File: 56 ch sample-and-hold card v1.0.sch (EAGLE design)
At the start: 124 parts, among them IC1 4051D, IC10 TL074JT, IC11 4051D, IC12 TL074JT, IC13 TL074JT, IC14 4051D, IC15 TL074JT, IC16 TL074JT, IC17 4051D, IC18 TL074JT, IC19 TL074JT, IC2 DAC8586D, IC20 4051D, IC21 TL074JT, IC22 TL074JT, IC26 4051D, IC27 TL074JT, IC28 TL074JT, IC3 TL074JT, IC5 78L05F, IC6 TL074JT, IC7 4051D, IC9 TL074JT, X2 FEMALE, X3 FEMALE, X4 FEMALE, X5 DNM, X6 DNM

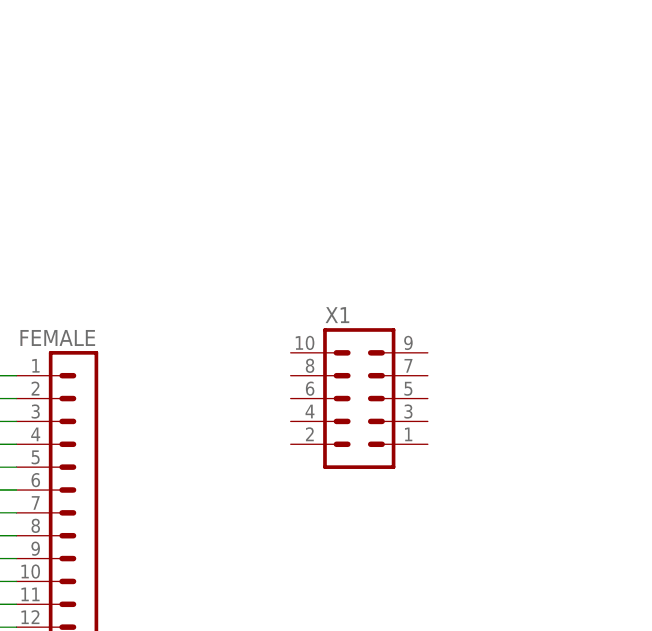
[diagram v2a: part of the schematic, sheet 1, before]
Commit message: All routed, nothing tested
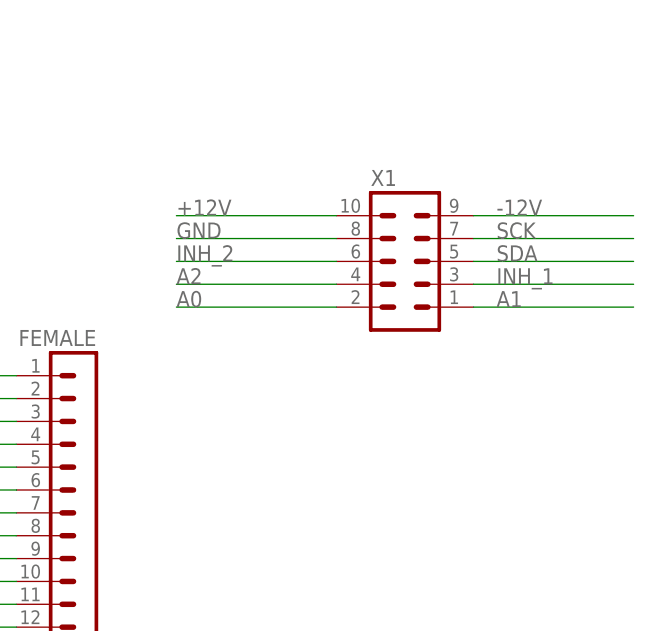
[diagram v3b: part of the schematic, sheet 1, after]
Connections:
- new net GND: X1.8
- net +12V: now also X1.10
- net -12V: now also X1.9
- net A0: now also X1.2
- net A1: now also X1.1
- net A2: now also X1.4
- net INH_1: now also X1.3
- net INH_2: now also X1.6
- net SCK: now also X1.7
- net SDA: now also X1.5
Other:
- moved on the sheet: X1
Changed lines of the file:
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@@
 <attribute name="VALUE" x="-2.54" y="71.12" size="1.778" layer="96"/>
 </instance>
-<instance part="X1" gate="G$1" x="129.54" y="-20.32" smashed="yes">
-<attribute name="VALUE" x="125.73" y="-30.48" size="1.778" layer="96"/>
-<attribute name="NAME" x="125.73" y="-11.938" size="1.778" layer="95"/>
+<instance part="X1" gate="G$1" x="134.62" y="-5.08" smashed="yes">
+<attribute name="VALUE" x="130.81" y="-15.24" size="1.778" layer="96"/>
+<attribute name="NAME" x="130.81" y="3.302" size="1.778" layer="95"/>
 </instance>
 <instance part="X2" gate="G$1" x="38.1" y="-35.56" smashed="yes" rot="R180">
@@
 <label x="55.88" y="22.86" size="1.778" layer="95"/>
 </segment>
+<segment>
+<pinref part="X1" gate="G$1" pin="9"/>
+<wire x1="142.24" y1="0" x2="160.02" y2="0" width="0.1524" layer="91"/>
+<label x="144.78" y="0" size="1.778" layer="95"/>
+</segment>
 </net>
 <net name="OUT_7" class="0">
@@
 <label x="55.88" y="25.4" size="1.778" layer="95"/>
 </segment>
+<segment>
+<pinref part="X1" gate="G$1" pin="10"/>
+<wire x1="127" y1="0" x2="109.22" y2="0" width="0.1524" layer="91"/>
+<label x="109.22" y="0" size="1.778" layer="95"/>
+</segment>
 </net>
 <net name="SCK" class="0">
@@
 <label x="55.88" y="17.78" size="1.778" layer="95"/>
 </segment>
+<segment>
+<pinref part="X1" gate="G$1" pin="7"/>
+<wire x1="142.24" y1="-2.54" x2="160.02" y2="-2.54" width="0.1524" layer="91"/>
+<label x="144.78" y="-2.54" size="1.778" layer="95"/>
+</segment>
 </net>
 <net name="SDA" class="0">
@@
 <label x="55.88" y="15.24" size="1.778" layer="95"/>
 </segment>
+<segment>
+<pinref part="X1" gate="G$1" pin="5"/>
+<wire x1="142.24" y1="-5.08" x2="160.02" y2="-5.08" width="0.1524" layer="91"/>
+<label x="144.78" y="-5.08" size="1.778" layer="95"/>
+</segment>
 </net>
 <net name="N$8" class="0">
@@
 <label x="55.88" y="7.62" size="1.778" layer="95"/>
 </segment>
+<segment>
+<pinref part="X1" gate="G$1" pin="2"/>
+<wire x1="127" y1="-10.16" x2="109.22" y2="-10.16" width="0.1524" layer="91"/>
+<label x="109.22" y="-10.16" size="1.778" layer="95"/>
+</segment>
 </net>
 <net name="A1" class="0">
@@
 <label x="55.88" y="5.08" size="1.778" layer="95"/>
 </segment>
+<segment>
+<pinref part="X1" gate="G$1" pin="1"/>
+<wire x1="142.24" y1="-10.16" x2="160.02" y2="-10.16" width="0.1524" layer="91"/>
+<label x="144.78" y="-10.16" size="1.778" layer="95"/>
+</segment>
 </net>
 <net name="A2" class="0">
@@
 <label x="55.88" y="2.54" size="1.778" layer="95"/>
 </segment>
+<segment>
+<pinref part="X1" gate="G$1" pin="4"/>
+<wire x1="127" y1="-7.62" x2="109.22" y2="-7.62" width="0.1524" layer="91"/>
+<label x="109.22" y="-7.62" size="1.778" layer="95"/>
+</segment>
 </net>
 <net name="INH_1" class="0">
@@
 <label x="55.88" y="0" size="1.778" layer="95"/>
 </segment>
+<segment>
+<pinref part="X1" gate="G$1" pin="3"/>
+<wire x1="142.24" y1="-7.62" x2="160.02" y2="-7.62" width="0.1524" layer="91"/>
+<label x="144.78" y="-7.62" size="1.778" layer="95"/>
+</segment>
 </net>
 <net name="INH_2" class="0">
@@
 <wire x1="55.88" y1="-2.54" x2="86.36" y2="-2.54" width="0.1524" layer="91"/>
 <label x="55.88" y="-2.54" size="1.778" layer="95"/>
+</segment>
+<segment>
+<pinref part="X1" gate="G$1" pin="6"/>
+<wire x1="127" y1="-5.08" x2="109.22" y2="-5.08" width="0.1524" layer="91"/>
+<label x="109.22" y="-5.08" size="1.778" layer="95"/>
 </segment>
 </net>
@@
 </segment>
 </net>
+<net name="GND" class="0">
+<segment>
+<pinref part="X1" gate="G$1" pin="8"/>
+<wire x1="127" y1="-2.54" x2="109.22" y2="-2.54" width="0.1524" layer="91"/>
+<label x="109.22" y="-2.54" size="1.778" layer="95"/>
+</segment>
+</net>

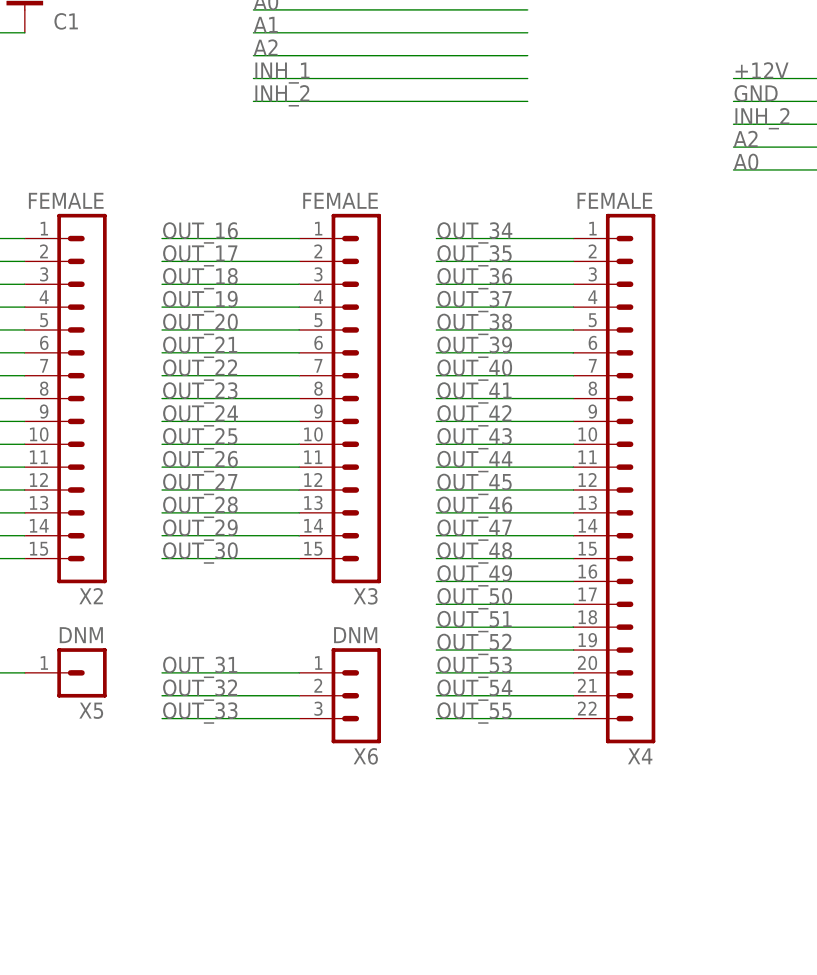
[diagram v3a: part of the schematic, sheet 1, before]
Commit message: Split 22p into 15p and 7p
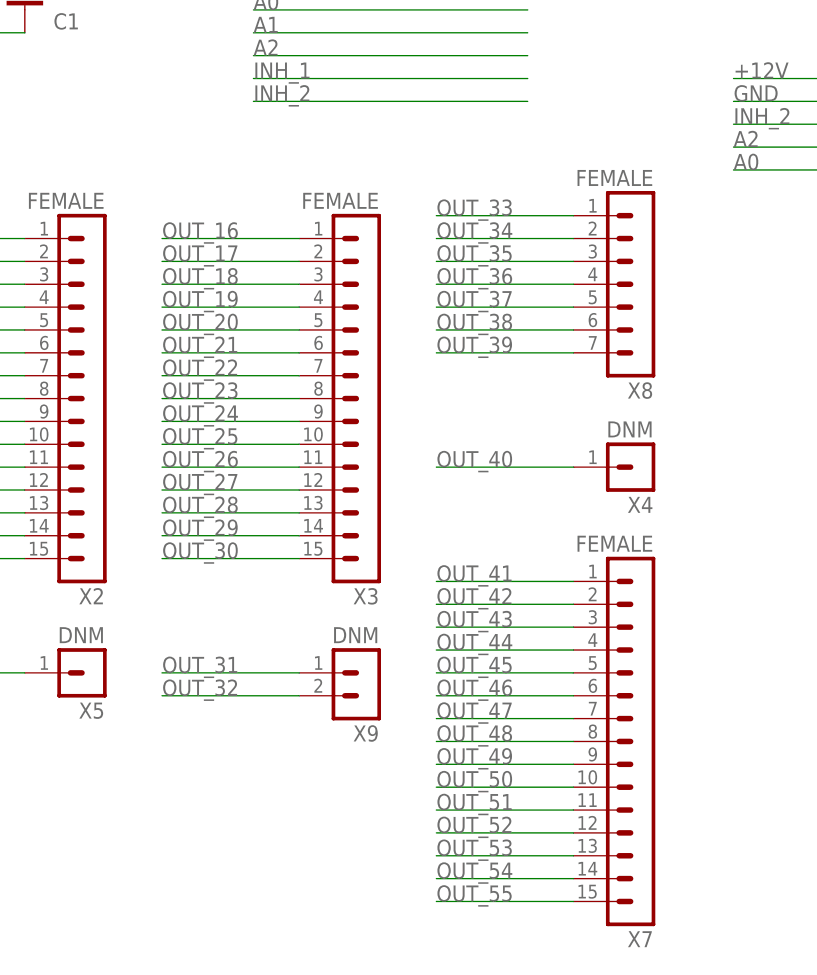
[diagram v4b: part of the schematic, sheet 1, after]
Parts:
- removed X6: DNM, joakim:MA03-1JN
- added X7: FEMALE, joakim:MA15-1JC
- added X8: FEMALE, joakim:MA07-1JC
- added X9: DNM, joakim:MA02-1JC
- IC1, IC11, IC14, IC17, IC20, IC26, IC7: value 4051D -> 74HCT4051D
- X4: value FEMALE -> DNM; device joakim:MA22-1JC -> joakim:MA01-1JN
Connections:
- net OUT_31: now also X9.1; no longer X6.1
- net OUT_32: now also X9.2; no longer X6.2
- net OUT_33: now also X8.1; no longer X6.3
- net OUT_34: now also X8.2; no longer X4.1
- net OUT_35: now also X8.3; no longer X4.2
- net OUT_36: now also X8.4; no longer X4.3
- net OUT_37: now also X8.5; no longer X4.4
- net OUT_38: now also X8.6; no longer X4.5
- net OUT_39: now also X8.7; no longer X4.6
- net OUT_40: now also X4.1; no longer X4.7
- net OUT_41: now also X7.1; no longer X4.8
- net OUT_42: now also X7.2; no longer X4.9
- net OUT_43: now also X7.3; no longer X4.10
- net OUT_44: now also X7.4; no longer X4.11
- net OUT_45: now also X7.5; no longer X4.12
- net OUT_46: now also X7.6; no longer X4.13
- net OUT_47: now also X7.7; no longer X4.14
- net OUT_48: now also X7.8; no longer X4.15
- net OUT_49: now also X7.9; no longer X4.16
- net OUT_50: now also X7.10; no longer X4.17
- net OUT_51: now also X7.11; no longer X4.18
- net OUT_52: now also X7.12; no longer X4.19
- net OUT_53: now also X7.13; no longer X4.20
- net OUT_54: now also X7.14; no longer X4.21
- net OUT_55: now also X7.15; no longer X4.22

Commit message: Switched to 2p nude
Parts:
- X9: device joakim:MA02-1JC -> joakim:MA02-1JN
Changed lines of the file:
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@@
 <part name="X8" library="joakim" deviceset="MA07-1J" device="C" value="FEMALE"/>
 <part name="X4" library="joakim" deviceset="MA01-1J" device="N" value="DNM"/>
-<part name="X9" library="joakim" deviceset="MA02-1J" device="C" value="DNM"/>
+<part name="X9" library="joakim" deviceset="MA02-1J" device="N" value="DNM"/>
 </parts>
 <sheets>

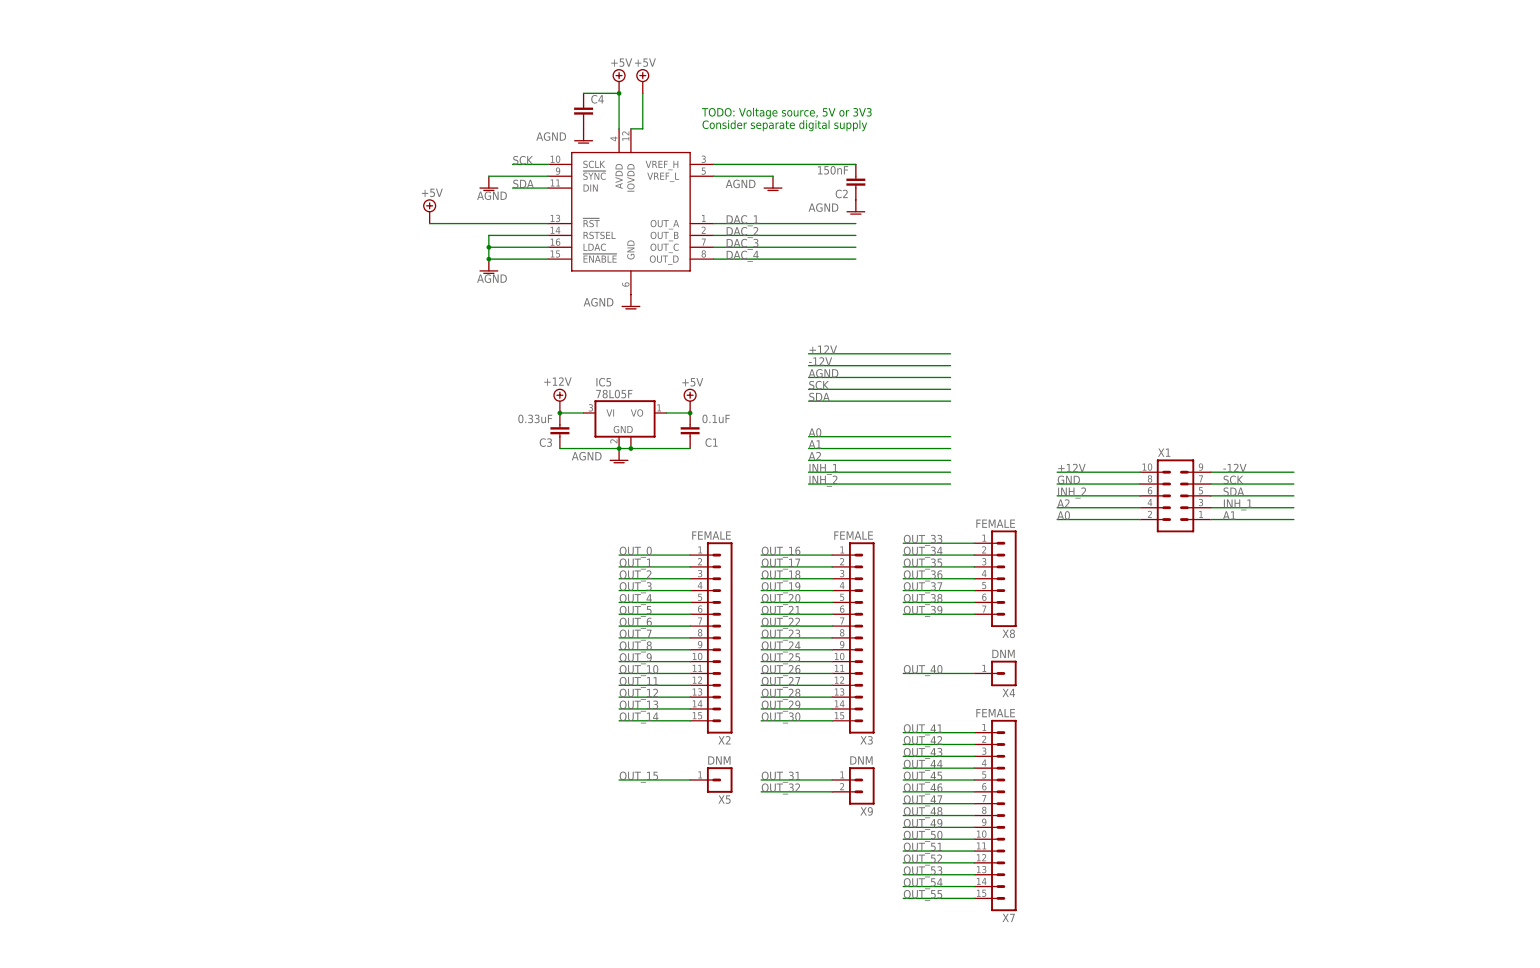
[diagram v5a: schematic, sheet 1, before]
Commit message: Switched to internal reference and buffering
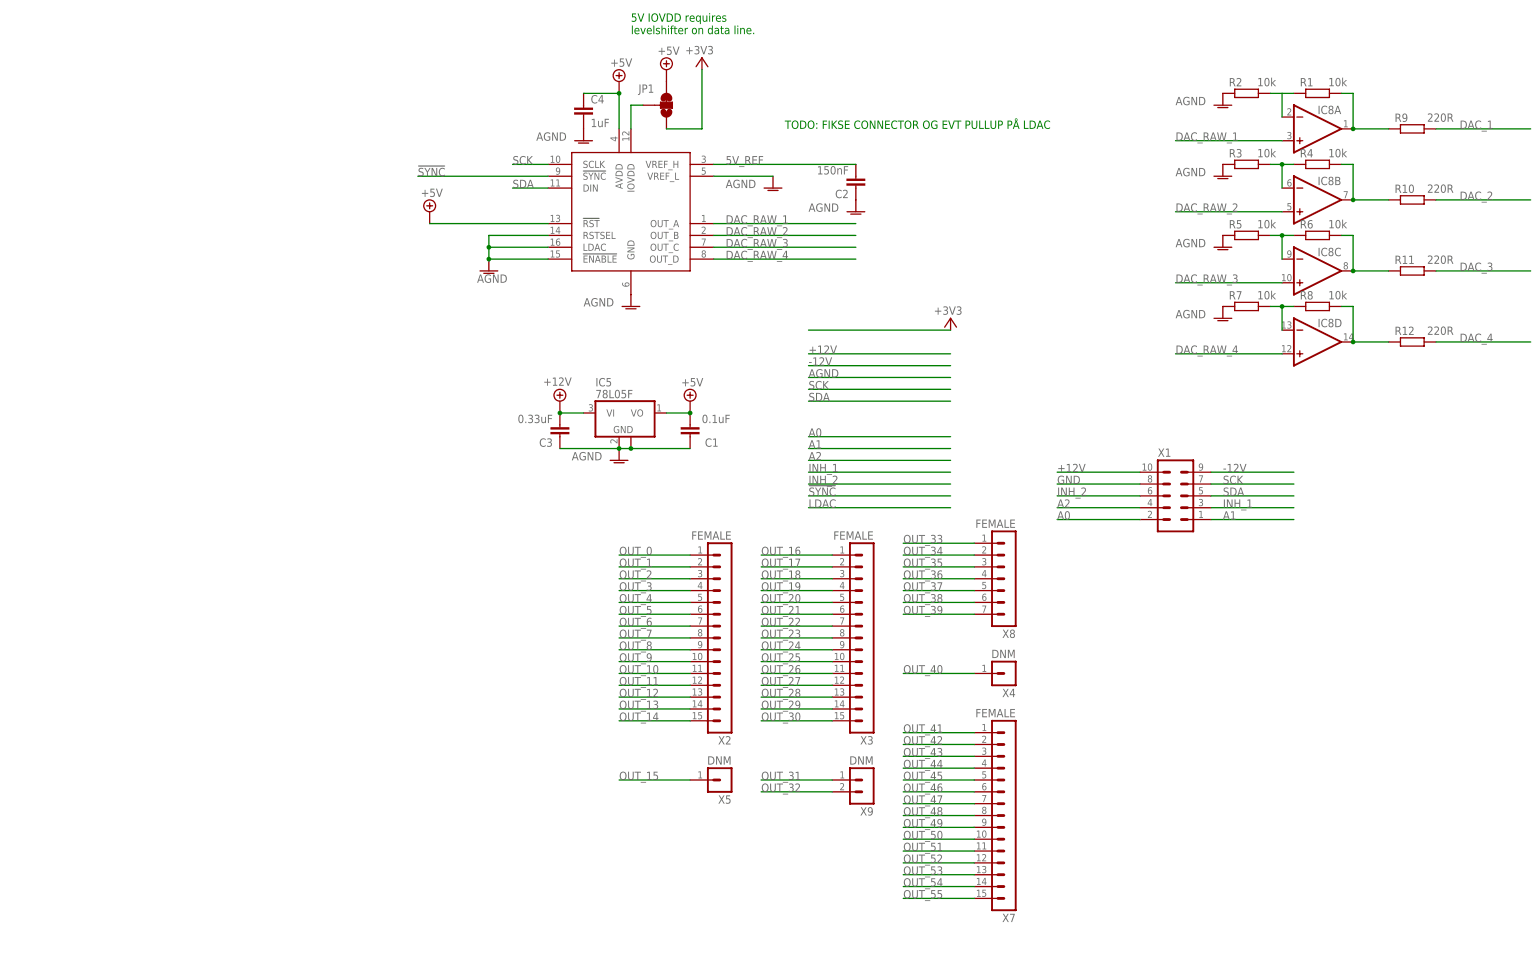
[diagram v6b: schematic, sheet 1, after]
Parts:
- added IC8: TL074JT, joakim:TL074JT
- added JP1: JUMPER-SMT_3_1-NC_TRACE_NO-SILK_DNM, SparkFun-Jumpers:JUMPER-SMT_3_1-NC_TRACE_NO-SILK
- added R1, R2, R3, R4, R5, R6, R7, R8: 10k, rcl:R-EU_R0603
- added R10, R11, R12, R9: 220R, rcl:R-EU_R0603
- C4: value (none) -> 1uF
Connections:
- net N$8 renamed 5V_REF
- new net !SYNC: IC2.!SYNC
- new net +3V3: JP1.1
- new net DAC_BUF_1: IC8A.OUT, R1.2, R9.1
- new net DAC_BUF_2: IC8B.OUT, R10.1, R4.2
- new net DAC_BUF_3: IC8C.OUT, R11.1, R6.2
- new net DAC_BUF_4: IC8D.OUT, R12.1, R8.2
- new net DAC_RAW_1: IC2.OUT_A, IC8A.+IN
- new net DAC_RAW_2: IC2.OUT_B, IC8B.+IN
- new net DAC_RAW_3: IC2.OUT_C, IC8C.+IN
- new net DAC_RAW_4: IC2.OUT_D, IC8D.+IN
- new net N$1: IC2.IOVDD, JP1.2
- new net N$2: IC8A.-IN
- new net N$3: IC8B.-IN, R3.2, R4.1
- new net N$4: IC8C.-IN, R5.2, R6.1
- new net N$5: IC8D.-IN, R7.2, R8.1
- new net N$6: R1.1, R2.2
- net +5V: now also JP1.3; no longer IC2.IOVDD
- net AGND: now also R2.1, R3.1, R5.1, R7.1; no longer IC2.!SYNC
- net DAC_1: now also R9.2; no longer IC2.OUT_A
- net DAC_2: now also R10.2; no longer IC2.OUT_B
- net DAC_3: now also R11.2; no longer IC2.OUT_C
- net DAC_4: now also R12.2; no longer IC2.OUT_D
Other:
- note added: "5V IOVDD requires levelshifter on data line."
- note added: "TODO: FIKSE CONNECTOR OG EVT PULLUP PÅ LDAC"
- note removed: "TODO: Voltage source, 5V or 3V3 Consider separate digital supply"
